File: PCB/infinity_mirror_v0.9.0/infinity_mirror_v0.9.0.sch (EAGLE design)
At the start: 31 parts, among them J1 POWER_JACKPTH_BREAD, J2 LED_CAP, J3 SERIAL, Q3 BSS138, U1 3.3LDO

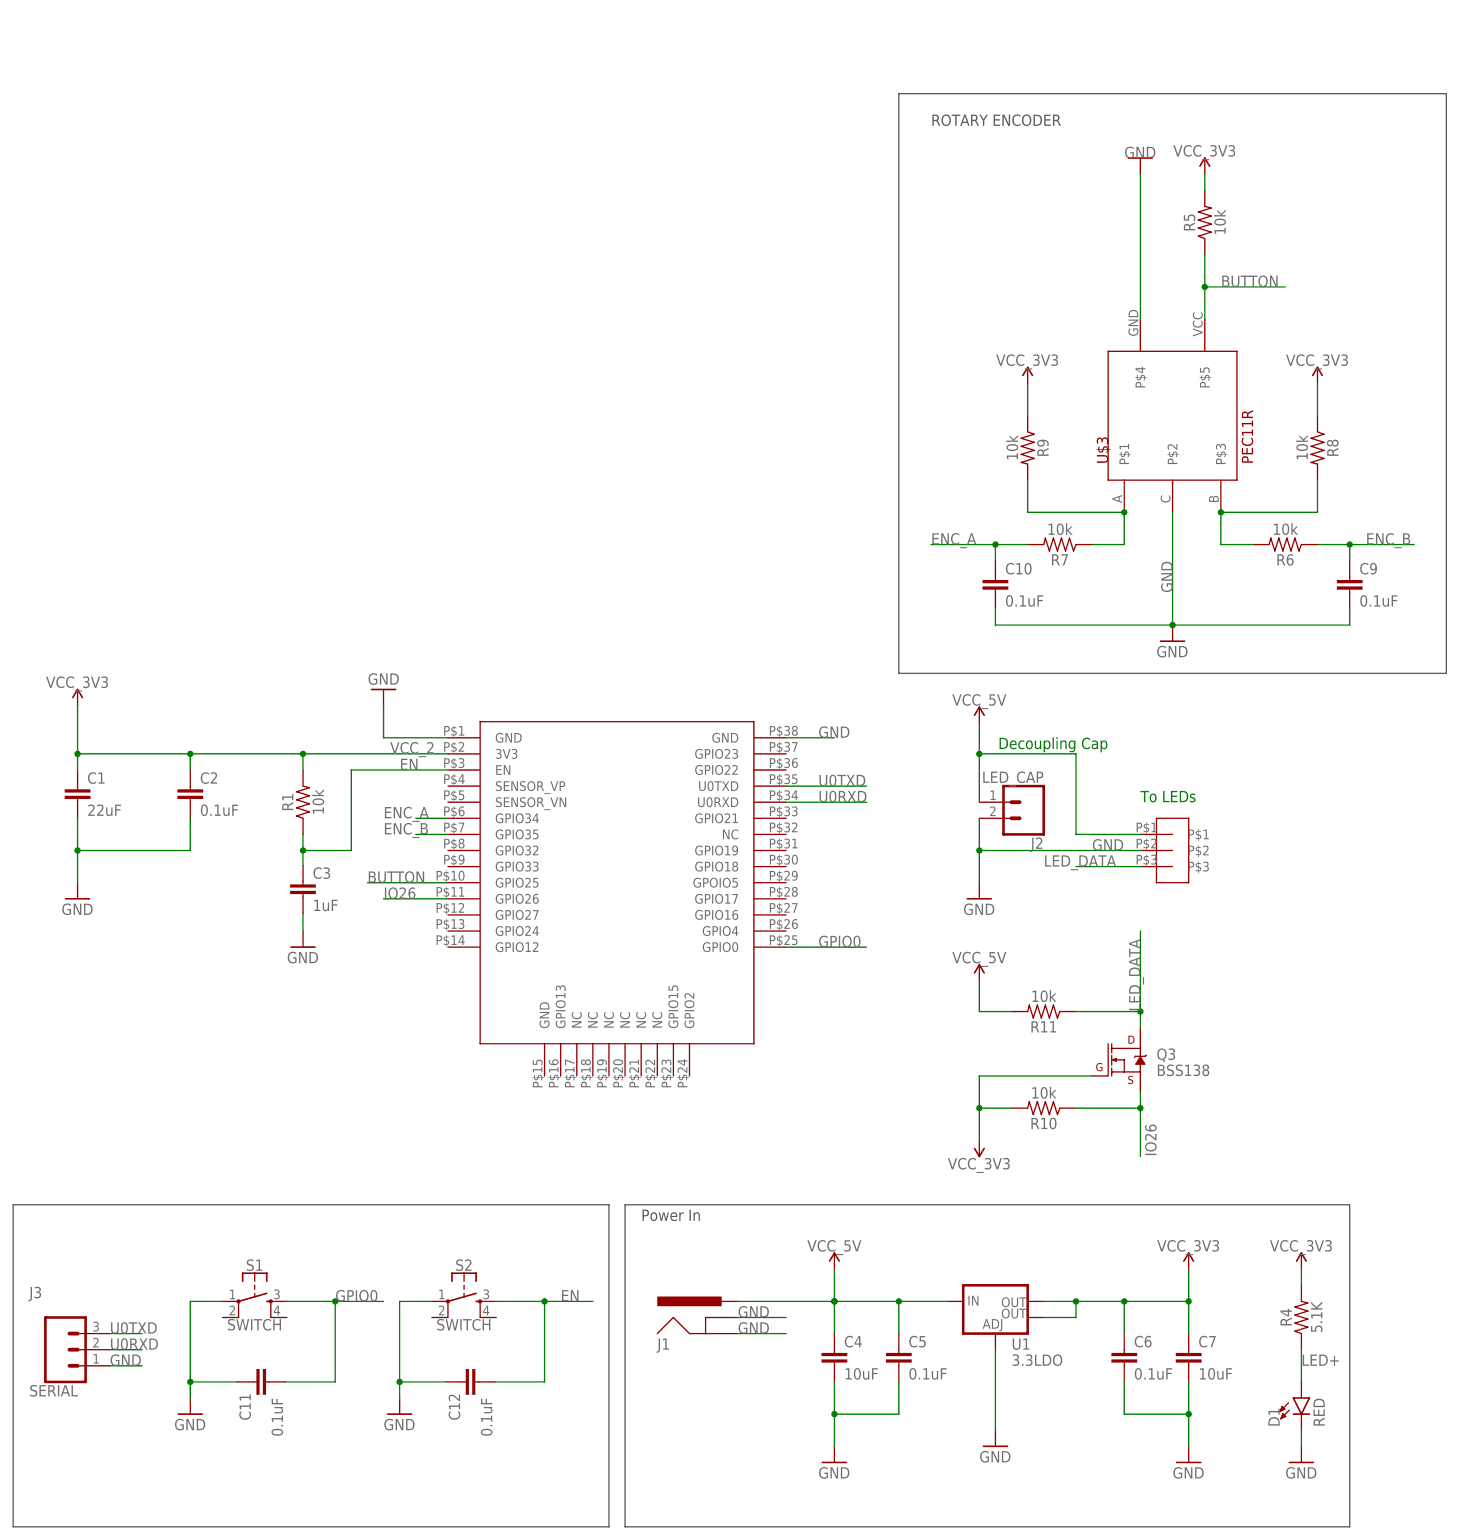
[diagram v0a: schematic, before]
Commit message: renamed v1.0.0 to v0.9.0, created BoM
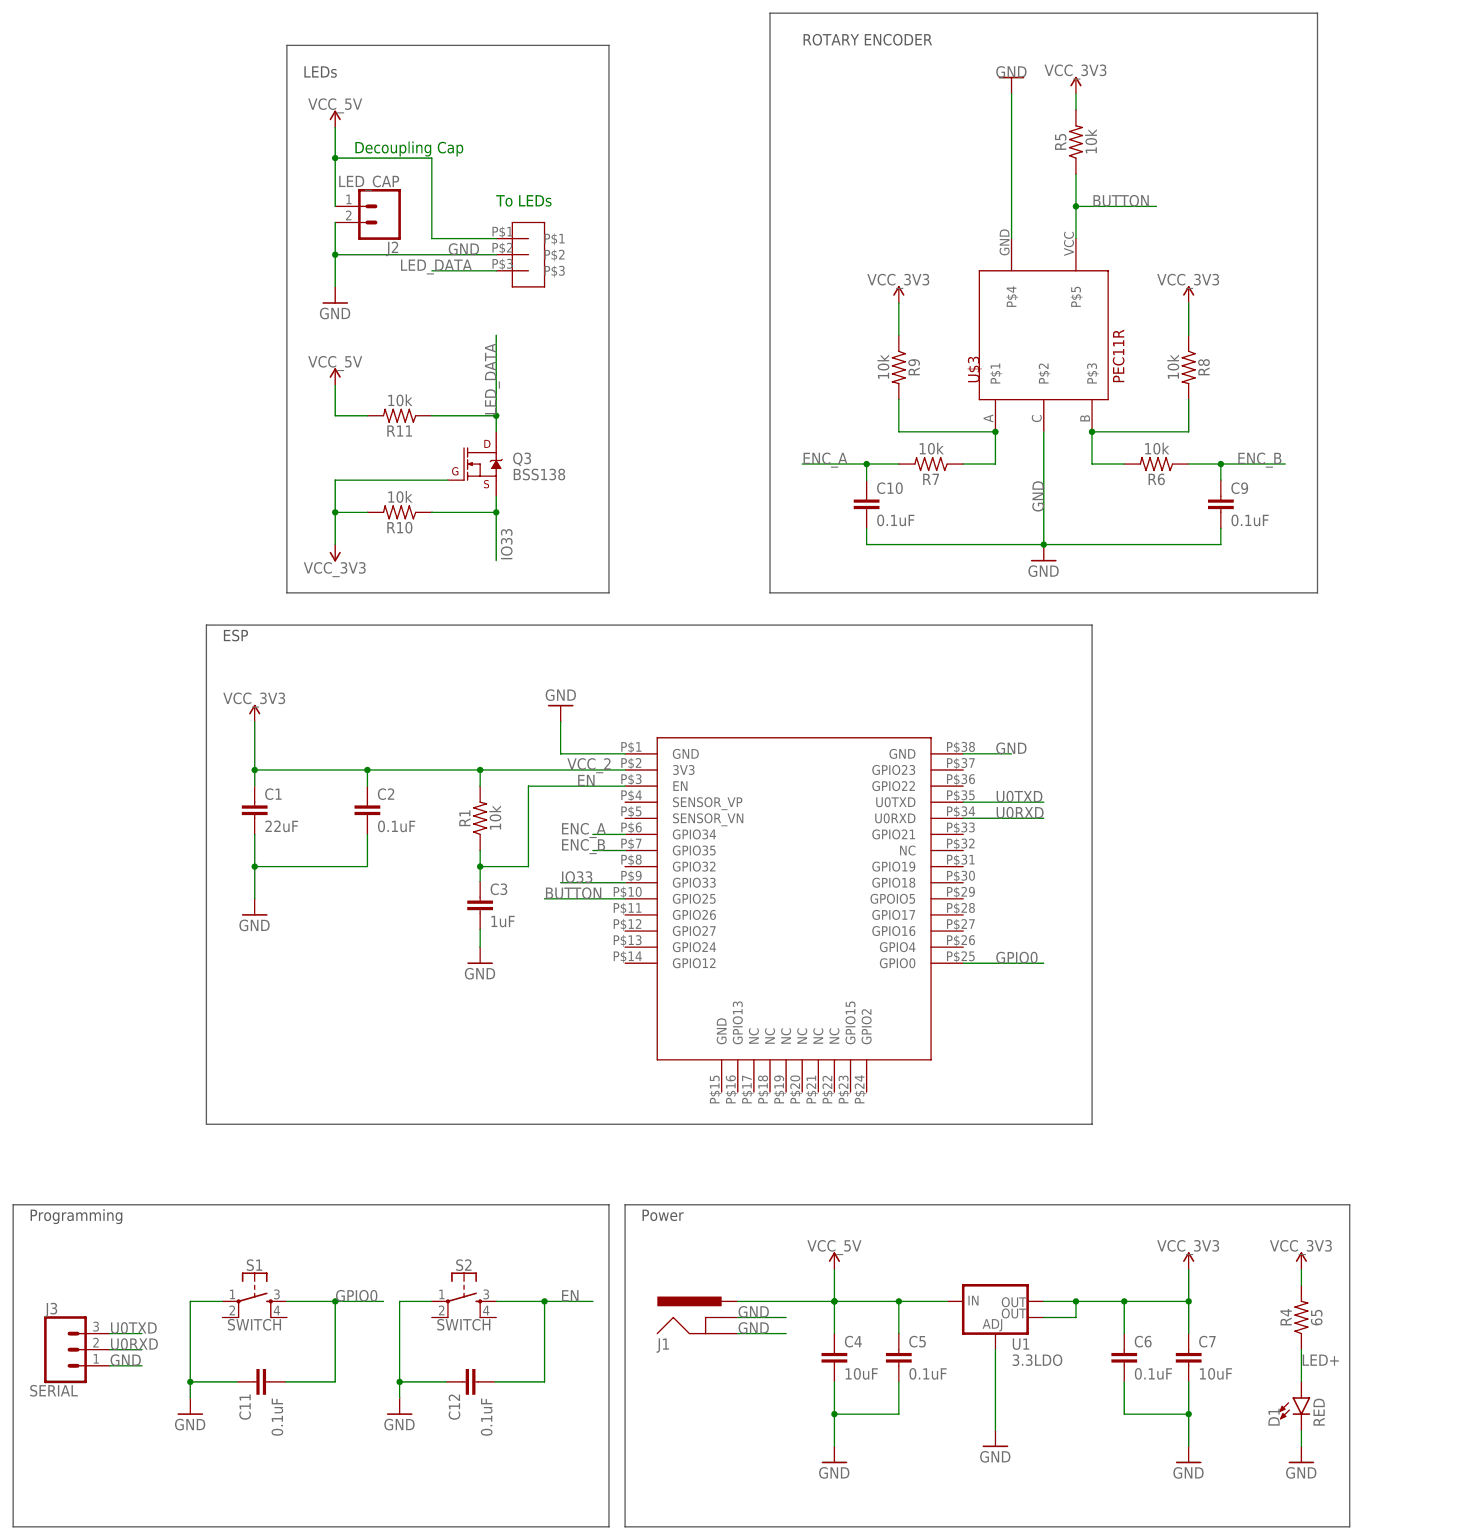
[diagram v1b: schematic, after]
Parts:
- R4: value 5.1K -> 65
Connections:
- removed net IO26: Q3.S, R10.1, U$1.GPIO26
- new net IO33: Q3.S, R10.1, U$1.GPIO33
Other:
- note added: "ESP"
- note added: "LEDs"
- note added: "Power"
- note added: "Programming"
- note removed: "Power In"
- moved on the sheet: C1, C10, C2, C3, C9, J2, Q3, R1, R10, R11, R5, R6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
